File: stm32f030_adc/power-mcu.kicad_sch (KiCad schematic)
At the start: 24 parts, among them J1 SWD, U1 STM32F103C6Tx, U2 AMS1117-3.3, X1 USB_B_Micro, Y1 8 MHz

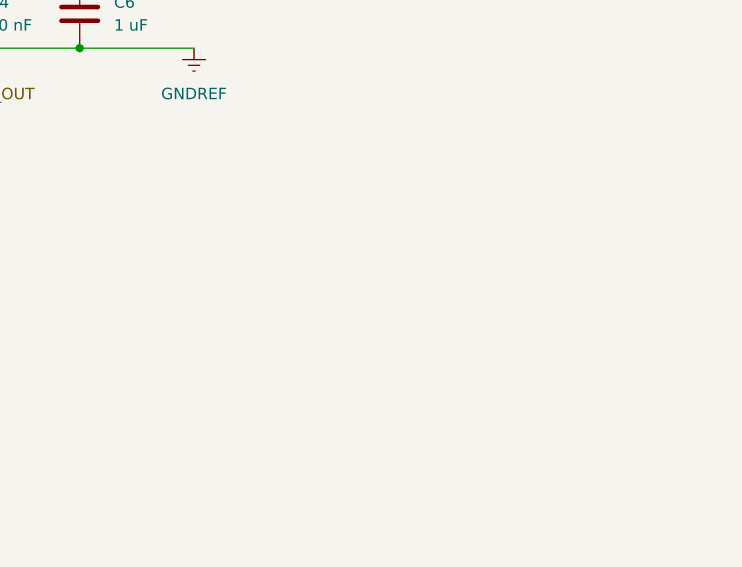
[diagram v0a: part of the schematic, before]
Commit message: [bjt-amp-calc schematics] Enh | Modified consulting the prototype
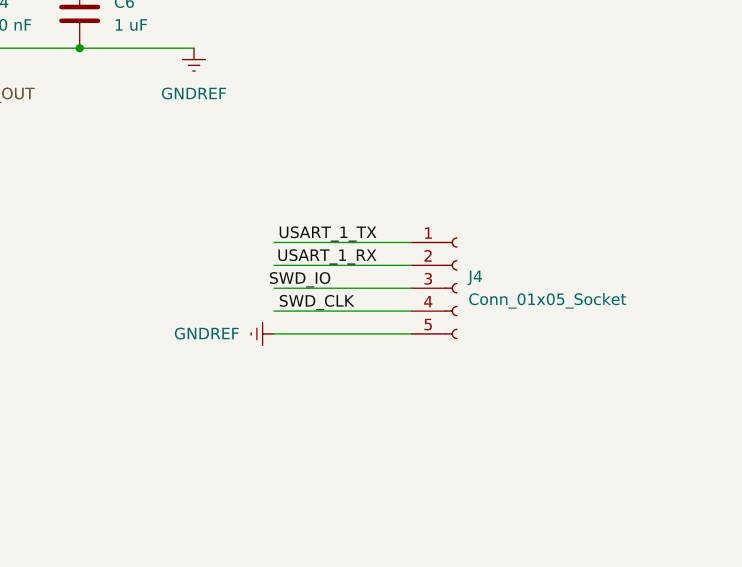
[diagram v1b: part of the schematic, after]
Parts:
- added J4: Conn_01x05_Socket, symbol Connector:Conn_01x05_Socket
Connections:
- net GNDREF: now also J4.5 (Pin_5)
- net SWD_CLK: now also J4.4 (Pin_4)
- net SWD_IO: now also J4.3 (Pin_3)
- net USART_1_RX: now also J4.2 (Pin_2)
- net USART_1_TX: now also J4.1 (Pin_1)
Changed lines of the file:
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@@
 	(wire
 		(pts
+			(xy 228.6 123.19) (xy 243.84 123.19)
+		)
+		(stroke
+			(width 0)
+			(type default)
+		)
+	)
+	(wire
+		(pts
 			(xy 44.45 58.42) (xy 44.45 59.69)
 		)
@@
 	(wire
 		(pts
+			(xy 228.6 115.57) (xy 243.84 115.57)
+		)
+		(stroke
+			(width 0)
+			(type default)
+		)
+	)
+	(wire
+		(pts
 			(xy 193.04 82.55) (xy 207.01 82.55)
 		)
@@
 	(wire
 		(pts
+			(xy 228.6 118.11) (xy 243.84 118.11)
+		)
+		(stroke
+			(width 0)
+			(type default)
+		)
+	)
+	(wire
+		(pts
 			(xy 68.58 146.05) (xy 81.28 146.05)
 		)
@@
 	(wire
 		(pts
+			(xy 228.6 125.73) (xy 243.84 125.73)
+		)
+		(stroke
+			(width 0)
+			(type default)
+		)
+	)
+	(wire
+		(pts
 			(xy 44.45 59.69) (xy 44.45 60.96)
 		)
@@
 	(wire
 		(pts
+			(xy 228.6 120.65) (xy 243.84 120.65)
+		)
+		(stroke
+			(width 0)
+			(type default)
+		)
+	)
+	(wire
+		(pts
 			(xy 55.88 43.18) (xy 52.07 43.18)
 		)
@@
 		)
 	)
+	(label "USART_1_TX"
+		(at 240.03 115.57 180)
+		(fields_autoplaced yes)
+		(effects
+			(font
+				(size 1.27 1.27)
+			)
+			(justify right bottom)
+		)
+	)
 	(label "USB_D-"
 		(at 77.47 50.8 0)
@@
 		)
 	)
+	(label "USART_1_RX"
+		(at 240.03 118.11 180)
+		(fields_autoplaced yes)
+		(effects
+			(font
+				(size 1.27 1.27)
+			)
+			(justify right bottom)
+		)
+	)
 	(label "SWD_3V3"
 		(at 64.77 95.25 180)
@@
 		)
 	)
+	(label "SWD_IO"
+		(at 234.95 120.65 180)
+		(fields_autoplaced yes)
+		(effects
+			(font
+				(size 1.27 1.27)
+			)
+			(justify right bottom)
+		)
+	)
 	(label "SWD_GND"
 		(at 64.77 97.79 180)
@@
 	)
 	(label "SWD_CLK"
+		(at 237.49 123.19 180)
+		(fields_autoplaced yes)
+		(effects
+			(font
+				(size 1.27 1.27)
+			)
+			(justify right bottom)
+		)
+	)
+	(label "SWD_CLK"
 		(at 198.12 132.08 180)
 		(fields_autoplaced yes)
@@
 	(symbol
 		(lib_id "power:GNDREF")
+		(at 228.6 125.73 270)
+		(unit 1)
+		(exclude_from_sim no)
+		(in_bom yes)
+		(on_board yes)
+		(dnp no)
+		(fields_autoplaced yes)
+		(property "Reference" "#PWR030"
+			(at 222.25 125.73 0)
+			(effects
+				(font
+					(size 1.27 1.27)
+				)
+				(hide yes)
+			)
+		)
+		(property "Value" "GNDREF"
+			(at 224.79 125.7299 90)
+			(effects
+				(font
+					(size 1.27 1.27)
+				)
+				(justify right)
+			)
+		)
+		(property "Footprint" ""
+			(at 228.6 125.73 0)
+			(effects
+				(font
+					(size 1.27 1.27)
+				)
+				(hide yes)
+			)
+		)
+		(property "Datasheet" ""
+			(at 228.6 125.73 0)
+			(effects
+				(font
+					(size 1.27 1.27)
+				)
+				(hide yes)
+			)
+		)
+		(property "Description" ""
+			(at 228.6 125.73 0)
+			(effects
+				(font
+					(size 1.27 1.27)
+				)
+				(hide yes)
+			)
+		)
+		(pin "1"
+		)
+		(instances
+			(project "stm32f030_adc"
+				(path "/85629656-c73b-4e1f-b8e8-4366f4b01266/961be52f-ca6e-47db-97af-a75ea0ab8933"
+					(reference "#PWR030")
+					(unit 1)
+				)
+			)
+		)
+	)
+	(symbol
+		(lib_id "power:GNDREF")
 		(at 60.96 171.45 0)
 		(unit 1)
@@
 					(unit 1)
 				)
+			)
+		)
+	)
+	(symbol
+		(lib_id "Connector:Conn_01x05_Socket")
+		(at 248.92 120.65 0)
+		(unit 1)
+		(exclude_from_sim no)
+		(in_bom yes)
+		(on_board yes)
+		(dnp no)
+		(fields_autoplaced yes)
+		(property "Reference" "J4"
+			(at 250.19 119.3799 0)
+			(effects
+				(font
+					(size 1.27 1.27)
+				)
+				(justify left)
+			)
+		)
+		(property "Value" "Conn_01x05_Socket"
+			(at 250.19 121.9199 0)
+			(effects
+				(font
+					(size 1.27 1.27)
+				)
+				(justify left)
+			)
+		)
+		(property "Footprint" ""
+			(at 248.92 120.65 0)
+			(effects
+				(font
+					(size 1.27 1.27)
+				)
+				(hide yes)
+			)
+		)
+		(property "Datasheet" "~"
+			(at 248.92 120.65 0)
+			(effects
+				(font
+					(size 1.27 1.27)
+				)
+				(hide yes)
+			)
+		)
+		(property "Description" "Generic connector, single row, 01x05, script generated"
+			(at 248.92 120.65 0)
+			(effects
+				(font
+					(size 1.27 1.27)
+				)
+				(hide yes)
+			)
+		)
+		(pin "2"
+		)
+		(pin "5"
+		)
+		(pin "4"
+		)
+		(pin "3"
+		)
+		(pin "1"
+		)
+		(instances
+			(project ""
+				(path "/85629656-c73b-4e1f-b8e8-4366f4b01266/961be52f-ca6e-47db-97af-a75ea0ab8933"
+					(reference "J4")
+					(unit 1)
+				)

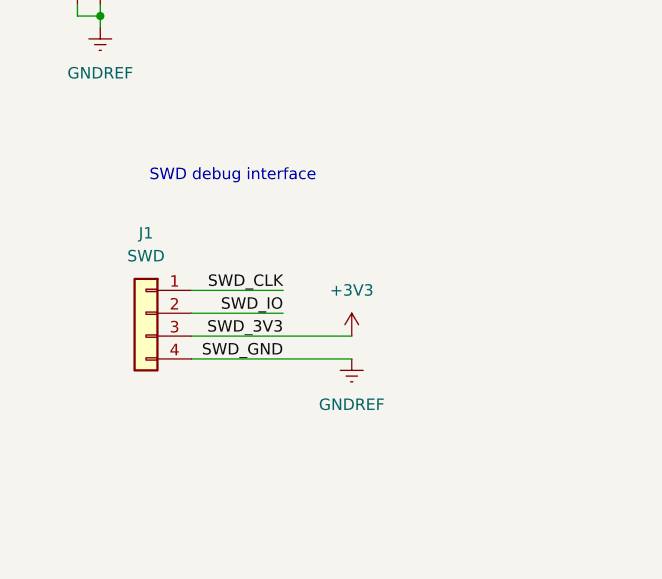
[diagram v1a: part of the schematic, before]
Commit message: Assigned footprints, removed obsolete parts
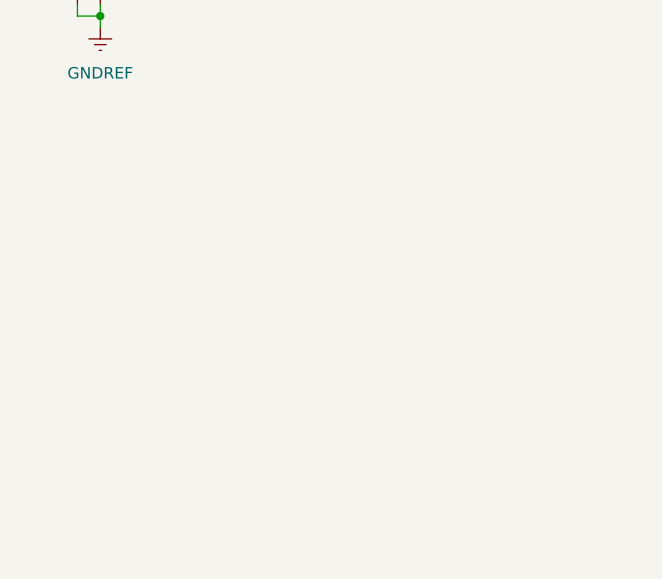
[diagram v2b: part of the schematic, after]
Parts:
- removed J1: SWD, symbol Connector_Generic:Conn_01x04
- C1, C10, C13, C14, C3, C4, C5, C6, C7, C8, C9: footprint (none) -> Capacitor_THT:CP_Axial_L10.0mm_D4.5mm_P15.00mm_Horizontal
- J4: footprint (none) -> Connector_PinHeader_2.00mm:PinHeader_1x05_P2.00mm_Vertical
- R1, R11, R2, R4, R5, R6, R7: footprint (none) -> Resistor_THT:R_Axial_DIN0207_L6.3mm_D2.5mm_P10.16mm_Horizontal
- X1: footprint (none) -> Connector_USB:USB_Micro-B_Wuerth_614105150721_Vertical
- Y1: footprint (none) -> Crystal:Resonator-2Pin_W6.0mm_H3.0mm
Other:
- note removed: "SWD debug interface"

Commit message: Layout: first approximation (grouping)
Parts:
- C2: footprint (none) -> Capacitor_THT:CP_Axial_L10.0mm_D4.5mm_P15.00mm_Horizontal
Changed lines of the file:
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@@
 			)
 		)
-		(property "Footprint" ""
+		(property "Footprint" "Capacitor_THT:CP_Axial_L10.0mm_D4.5mm_P15.00mm_Horizontal"
 			(at 176.2252 55.88 0)
 			(effects

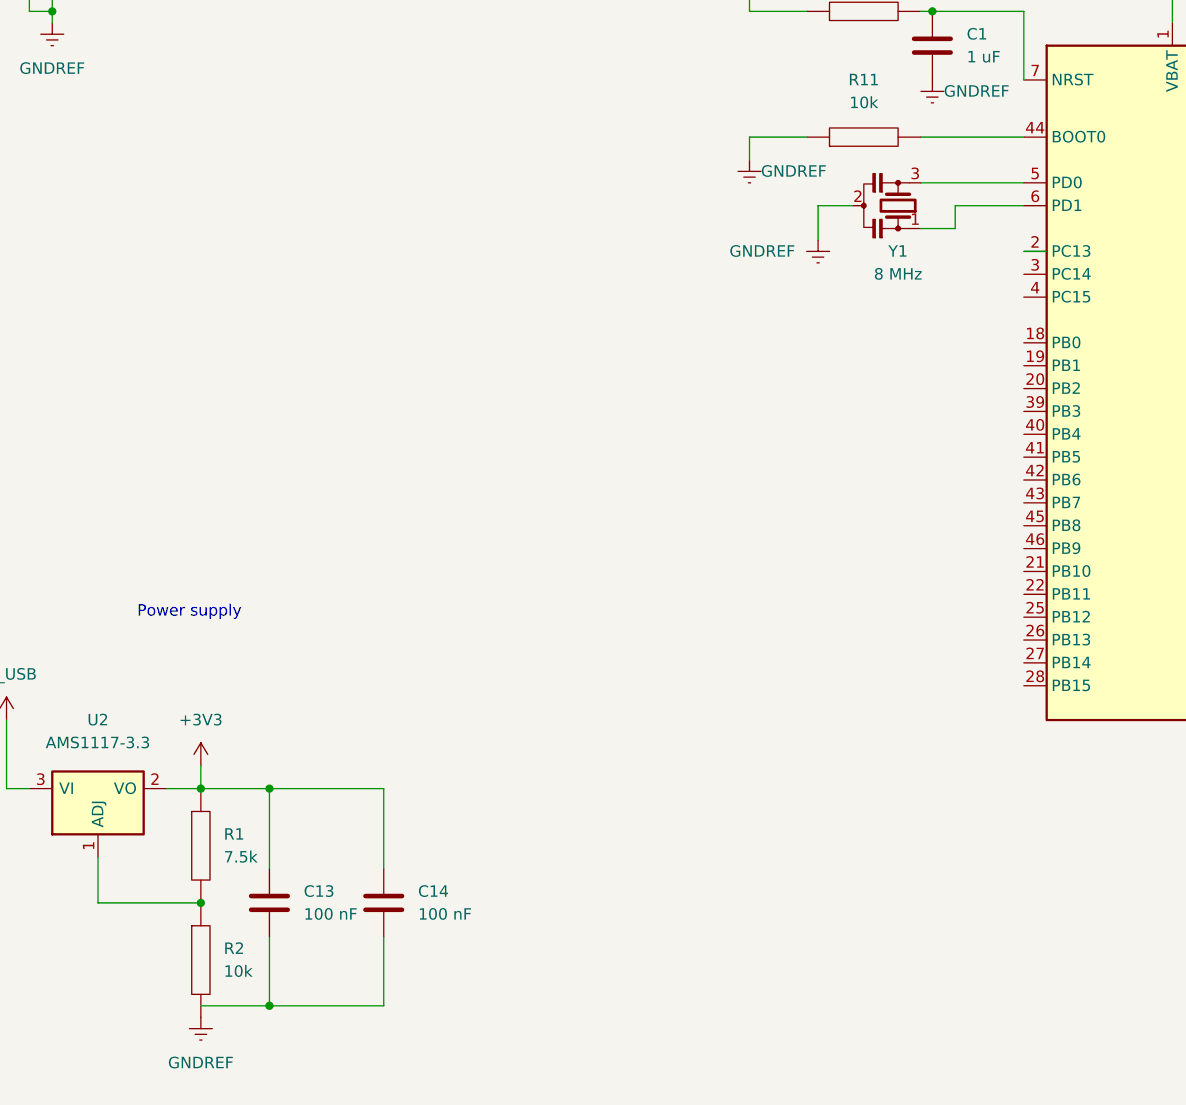
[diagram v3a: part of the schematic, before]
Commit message: [schematics] Build | Changed oscillator type, fixed unconnected lines, made some layout
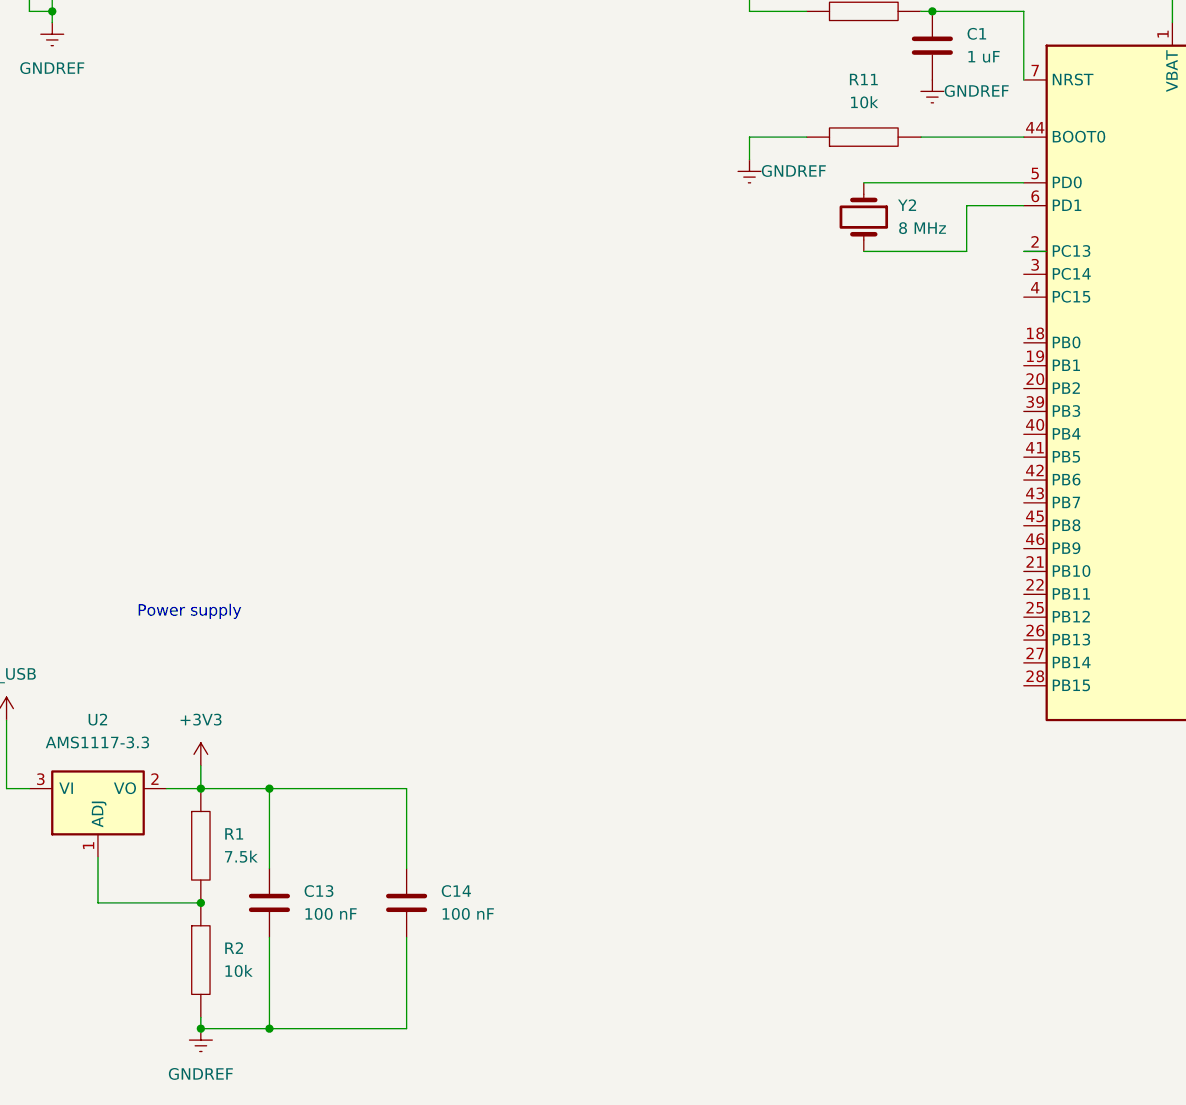
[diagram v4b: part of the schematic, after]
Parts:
- removed Y1: 8 MHz, Crystal:Resonator-2Pin_W6.0mm_H3.0mm, symbol Device:Resonator_Small
- added Y2: 8 MHz, Crystal:Resonator-2Pin_W6.0mm_H3.0mm, symbol Device:Crystal
- C1, C10, C13, C14, C2, C3, C4, C5, C6, C7, C8, C9: footprint Capacitor_THT:CP_Axial_L10.0mm_D4.5mm_P15.00mm_Horizontal -> Capacitor_THT:C_Disc_D4.7mm_W2.5mm_P5.00mm
- X1: footprint Connector_USB:USB_Micro-B_Wuerth_614105150721_Vertical -> Connector_USB:USB_Mini-B_Lumberg_2486_01_Horizontal
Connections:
- net GNDREF: now also C13.2, C14.2
- net at U1.5 (PD0): now also Y2.1
- net at U1.6 (PD1): now also Y2.2
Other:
- moved on the sheet: C14
